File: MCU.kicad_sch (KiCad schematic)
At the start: 71 parts, among them J401 EXPANSION_PORT, J402 RS485_1, J403 RS485_2, J404 Conn_ARM_JTAG_SWD_10, U401 74HC4094, U402 74HC4094, U403 EFM32PG22C200F512IM40, U404 SN75176AD, U405 XC6204B33, Y401 Abracon_ABM11

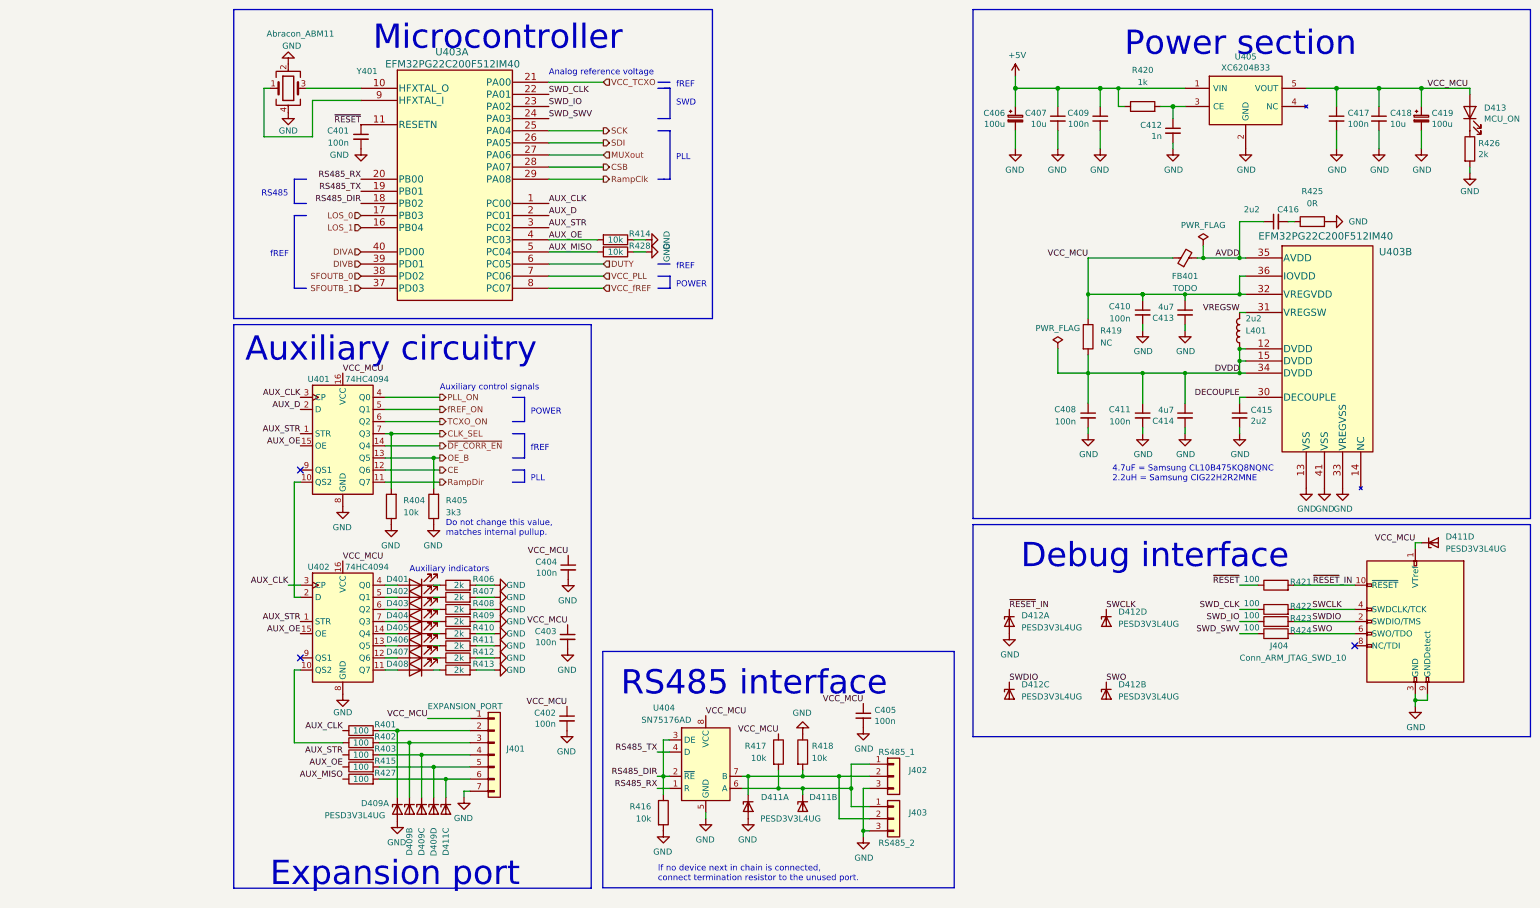
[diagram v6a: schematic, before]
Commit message: Partially reworked aux interface, about to be remade once again.
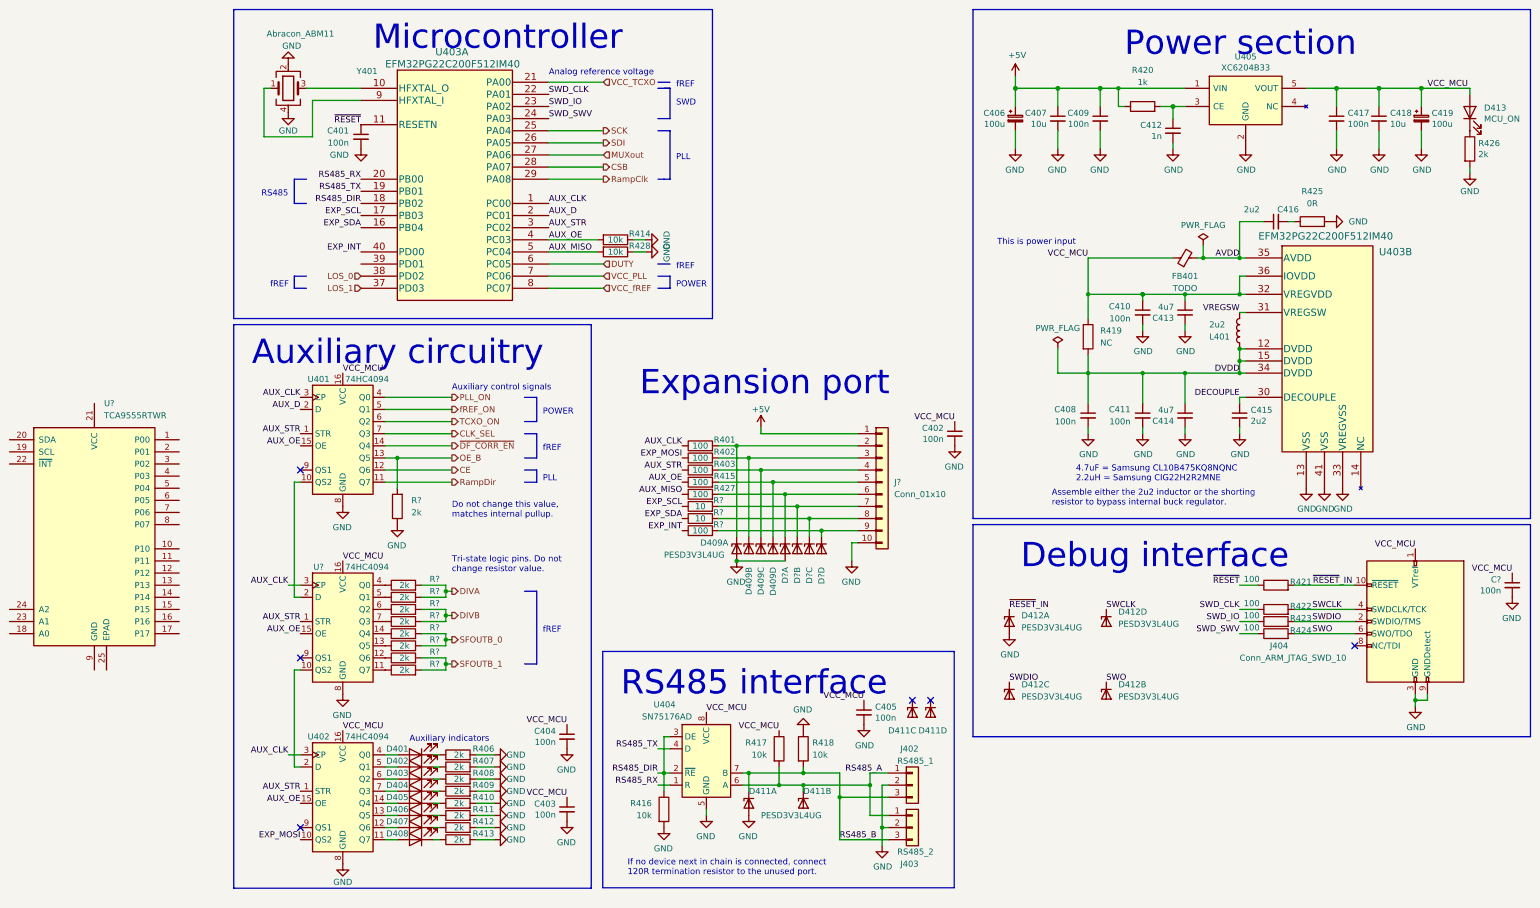
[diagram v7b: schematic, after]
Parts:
- removed J401: EXPANSION_PORT, Connector_PinHeader_2.54mm:PinHeader_1x07_P2.54mm_Vertical, symbol Connector_Generic:Conn_01x07
- removed R404: 10k, Resistor_SMD:R_0603_1608Metric_Pad0.98x0.95mm_HandSolder, symbol Device:R
- removed R405: 3k3, Resistor_SMD:R_0603_1608Metric_Pad0.98x0.95mm_HandSolder, symbol Device:R
- added C?: 100n, Capacitor_SMD:C_0603_1608Metric_Pad1.08x0.95mm_HandSolder, symbol Device:C_Small
- added D? (x4): PESD3V3L4UG, Package_TO_SOT_SMD:SOT-353_SC-70-5, symbol Power_Protection:PESD3V3L4UG
- added J?: Conn_01x10, Connector_FFC-FPC:TE_1-84952-0_1x10-1MP_P1.0mm_Horizontal, symbol Connector_Generic:Conn_01x10
- added R?: 100, Resistor_SMD:R_0603_1608Metric_Pad0.98x0.95mm_HandSolder, symbol Device:R
- added R? (x9): 2k, Resistor_SMD:R_0603_1608Metric_Pad0.98x0.95mm_HandSolder, symbol Device:R
- added R? (x2): 10, Resistor_SMD:R_0603_1608Metric_Pad0.98x0.95mm_HandSolder, symbol Device:R
- added U?: 74HC4094, Package_SO:SO-16_3.9x9.9mm_P1.27mm, symbol petr:74HC4094
- added U?: TCA9555RTWR, Package_DFN_QFN:WQFN-24-1EP_4x4mm_P0.5mm_EP2.45x2.45mm, symbol Interface_Expansion:TCA9555RTWR
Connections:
- net +5V: now also J?.1 (Pin_1)
- net AUX_CLK: now also U?.3 (CP)
- net AUX_OE: now also U?.15 (OE)
- net AUX_STR: now also U?.1 (STR)
- net DIVA: now also R?.2, R?.2; no longer U403.40 (PD00)
- net DIVB: now also R?.2, R?.2; no longer U403.39 (PD01)
- net GND: now also J402.2 (Pin_2), J403.2 (Pin_2), C?.2, D?.2 (A), J?.10 (Pin_10), R?.1, U?.8 (GND); no longer J402.3 (Pin_3), J403.3 (Pin_3)
- net LOS_0: now also U403.38 (PD02); no longer U403.17 (PB03)
- net LOS_1: now also U403.37 (PD03); no longer U403.16 (PB04)
- net OE_B: now also R?.2
- net SFOUTB_0: now also R?.2, R?.2; no longer U403.38 (PD02)
- net SFOUTB_1: now also R?.2, R?.2; no longer U403.37 (PD03)
- net VCC_MCU: now also C?.1, U?.16 (VCC); no longer D411.5 (K4)
- net at D409.1 (K1), R401.2: now also J?.2 (Pin_2)
- net EXP_MOSI: now reaches R402.1, U402.10 (QS2)
- net at U402.2 (D): now also U?.10 (QS2); no longer U401.10 (QS2)
- net RS485_A: now reaches D411.3 (K2), J402.1 (Pin_1), J403.1 (Pin_1), R417.2, U404.6 (A)
- net at D409.4 (K3), R403.2: now also J?.4 (Pin_4)
- net RS485_B: now reaches D411.1 (K1), R418.2, U404.7 (B)
- net RS485_B: now also J402.3 (Pin_3), J403.3 (Pin_3); no longer J402.2 (Pin_2), J403.2 (Pin_2)
- net at D409.5 (K4), R415.2: now also J?.5 (Pin_5)
- net at D409.3 (K2), R402.2: now also J?.3 (Pin_3)
- net at R427.2: now also D?.1 (K1), J?.6 (Pin_6); no longer D411.4 (K3)
- new net: D?.5 (K4), J?.9 (Pin_9), R?.2
- new net: R?.1, U?.11 (Q7)
- new net: R?.1, U?.12 (Q6)
- new net: R?.1, U?.13 (Q5)
- new net: R?.1, U?.14 (Q4)
- new net: U401.10 (QS2), U?.2 (D)
- new net: R?.1, U?.4 (Q0)
- new net: R?.1, U?.5 (Q1)
- new net: R?.1, U?.6 (Q2)
- new net: R?.1, U?.7 (Q3)
- new net: D?.4 (K3), J?.8 (Pin_8), R?.2
- new net: D?.3 (K2), J?.7 (Pin_7), R?.2
- new net EXP_INT: R?.1, U403.40 (PD00)
- new net EXP_SCL: R?.1, U403.17 (PB03)
- new net EXP_SDA: R?.1, U403.16 (PB04)
- no-connect marks 3 -> 6
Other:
- note added: "Assemble either the 2u2 inductor or the shorting resistor to bypass internal buck regulator."
- note added: "If no device next in chain is connected, connect 120R termination resistor to the unused port."
- note added: "This is power input"
- note added: "Tri-state logic pins. Do not change resistor value."
- note removed: "If no device next in chain is connected, connect termination resistor to the unused port."
- moved on the sheet: C402, C403, C404, C405, D401, D402, D403, D404, D405, D406, D407, D408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

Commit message: Remade and simplified AUX/EXT section.
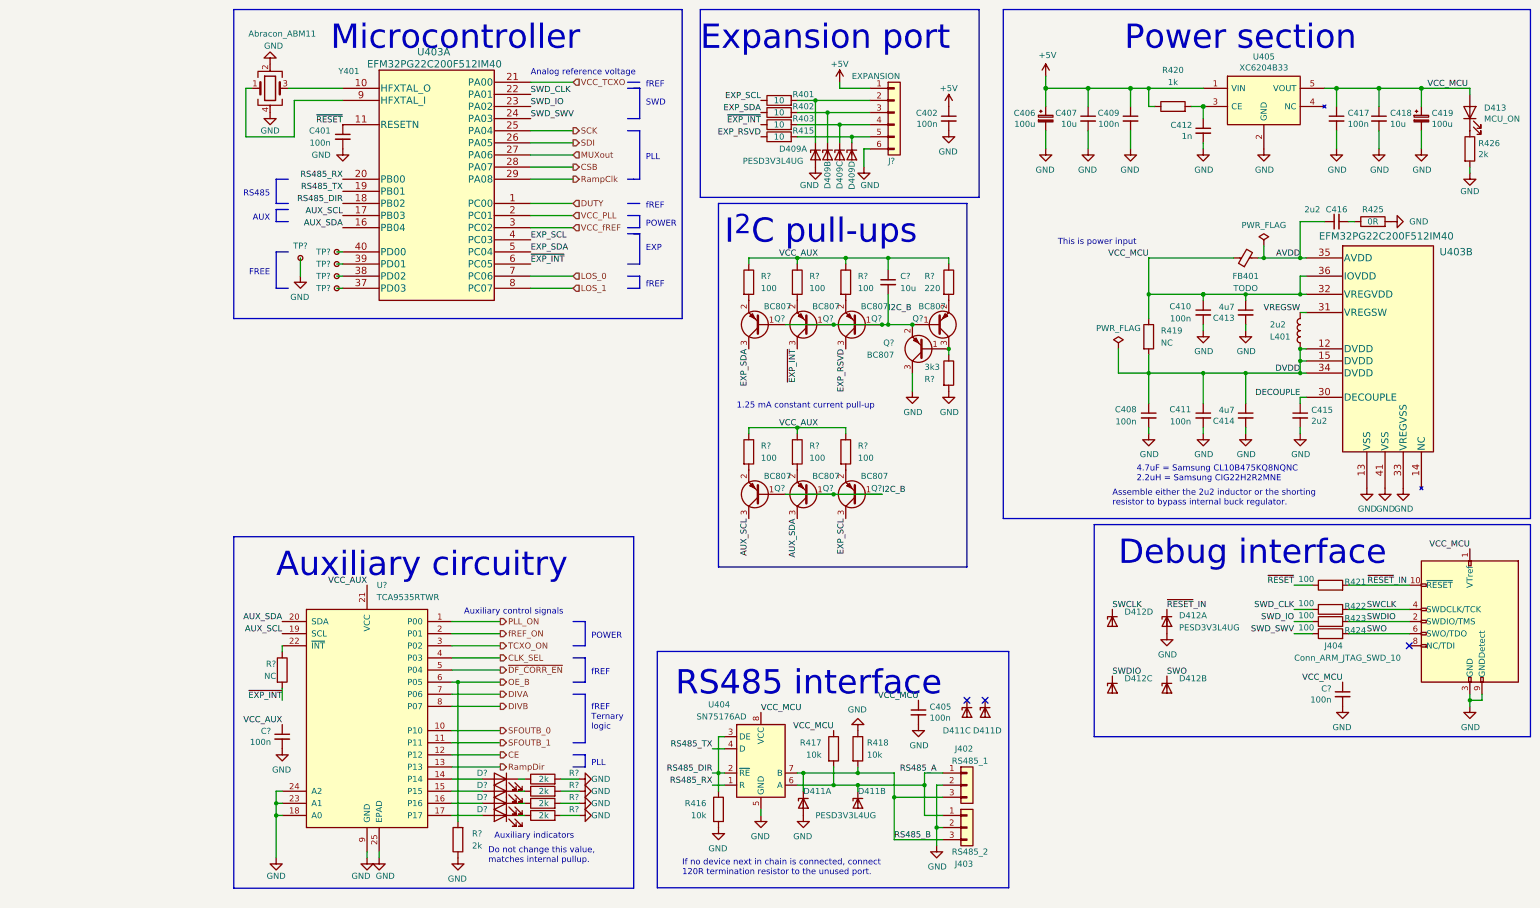
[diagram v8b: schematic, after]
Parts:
- removed C403, C404: 100n, Capacitor_SMD:C_0603_1608Metric_Pad1.08x0.95mm_HandSolder, symbol Device:C_Small
- removed D401, D402, D403, D404, D405, D406, D407, D408: (no value), LED_SMD:LED_0603_1608Metric_Pad1.05x0.95mm_HandSolder, symbol Device:LED
- removed D? (x4): PESD3V3L4UG, Package_TO_SOT_SMD:SOT-353_SC-70-5, symbol Power_Protection:PESD3V3L4UG
- removed J?: Conn_01x10, Connector_FFC-FPC:TE_1-84952-0_1x10-1MP_P1.0mm_Horizontal, symbol Connector_Generic:Conn_01x10
- removed R406, R407, R408, R409, R410, R411, R412, R413, R? (x9): 2k, Resistor_SMD:R_0603_1608Metric_Pad0.98x0.95mm_HandSolder, symbol Device:R
- removed R414, R428: 10k, Resistor_SMD:R_0603_1608Metric_Pad0.98x0.95mm_HandSolder, symbol Device:R
- removed R427, R?: 100, Resistor_SMD:R_0603_1608Metric_Pad0.98x0.95mm_HandSolder, symbol Device:R
- removed R? (x2): 10, Resistor_SMD:R_0603_1608Metric_Pad0.98x0.95mm_HandSolder, symbol Device:R
- removed U401, U402, U?: 74HC4094, Package_SO:SO-16_3.9x9.9mm_P1.27mm, symbol petr:74HC4094
- removed U?: TCA9555RTWR, Package_DFN_QFN:WQFN-24-1EP_4x4mm_P0.5mm_EP2.45x2.45mm, symbol Interface_Expansion:TCA9555RTWR
- added C?: 10u, Capacitor_SMD:C_0805_2012Metric_Pad1.18x1.45mm_HandSolder, symbol Device:C_Small
- added C?: 100n, Capacitor_SMD:C_0603_1608Metric_Pad1.08x0.95mm_HandSolder, symbol Device:C_Small
- added D? (x4): (no value), LED_SMD:LED_0603_1608Metric_Pad1.05x0.95mm_HandSolder, symbol Device:LED
- added J?: EXPANSION, Connector_FFC-FPC:TE_84952-6_1x06-1MP_P1.0mm_Horizontal, symbol Connector_Generic:Conn_01x06
- added Q? (x8): BC807, Package_TO_SOT_SMD:SOT-23, symbol Transistor_BJT:BC807
- added R?: NC, Resistor_SMD:R_0603_1608Metric_Pad0.98x0.95mm_HandSolder, symbol Device:R
- added R? (x6): 100, Resistor_SMD:R_0603_1608Metric_Pad0.98x0.95mm_HandSolder, symbol Device:R
- added R? (x5): 2k, Resistor_SMD:R_0603_1608Metric_Pad0.98x0.95mm_HandSolder, symbol Device:R
- added R?: 3k3, Resistor_SMD:R_0603_1608Metric_Pad0.98x0.95mm_HandSolder, symbol Device:R
- added R?: 220, Resistor_SMD:R_0603_1608Metric_Pad0.98x0.95mm_HandSolder, symbol Device:R
- added TP? (x5): TestPoint_Small, symbol 4ms_Connector:TestPoint_Small
- added U?: TCA9535RTWR, Package_DFN_QFN:WQFN-24-1EP_4x4mm_P0.5mm_EP2.45x2.45mm, symbol Interface_Expansion:TCA9535RTWR
- R401, R402, R403, R415: value 100 -> 10
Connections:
- net AUX_D is gone; now on net VCC_PLL: U403.2 (PC01)
- net AUX_MISO is gone; now on net EXP_SDA: U403.5 (PC04)
- net EXP_MOSI is gone; now on net EXP_SDA: R402.1
- net +5V: now also C402.1, J?.1 (Pin_1)
- net CE: now also U?.12 (P12)
- net CLK_SEL: now also U?.4 (P03)
- net DIVA: now also U?.7 (P06)
- net DIVB: now also U?.8 (P07)
- net DUTY: now also U403.1 (PC00); no longer U403.6 (PC05)
- net EXP_SCL: now also R401.1, U403.4 (PC03), Q?.3 (C); no longer U403.17 (PB03)
- net EXP_SDA: now also Q?.3 (C); no longer U403.16 (PB04)
- net GND: now also C?.2, J?.6 (Pin_6), Q?.3 (C), R?.1, R?.2, R?.2, R?.2, R?.2, R?.2, TP?.1, U?.18 (A0), U?.23 (A1), U?.24 (A2), U?.25 (EPAD), U?.9 (GND)
- net LOS_0: now also U403.7 (PC06); no longer U403.38 (PD02)
- net LOS_1: now also U403.8 (PC07); no longer U403.37 (PD03)
- net OE_B: now also R?.2, U?.6 (P05)
- net PLL_ON: now also U?.1 (P00)
- net RampDir: now also U?.13 (P13)
- net SFOUTB_0: now also U?.10 (P10)
- net SFOUTB_1: now also U?.11 (P11)
- net TCXO_ON: now also U?.3 (P02)
- net VCC_MCU: no longer C402.1
- net VCC_PLL: no longer U403.7 (PC06)
- net VCC_fREF: now also U403.3 (PC02); no longer U403.8 (PC07)
- net fREF_ON: now also U?.2 (P01)
- net ~{DF_CORR_EN}: now also U?.5 (P04)
- net at D409.1 (K1), R401.2: now also J?.2 (Pin_2)
- net at D409.4 (K3), R403.2: now also J?.4 (Pin_4)
- net at U403.39 (PD01): now also TP?.1
- net at D409.5 (K4), R415.2: now also J?.5 (Pin_5)
- net at D409.3 (K2), R402.2: now also J?.3 (Pin_3)
- removed net AUX_CLK: R401.1, U403.1 (PC00)
- net AUX_OE renamed EXP_RSVD
- net EXP_RSVD: now also Q?.3 (C); no longer U403.4 (PC03)
- net AUX_STR renamed ~{EXP_INT}
- net ~{EXP_INT}: now also U403.6 (PC05), Q?.3 (C), R?.2; no longer U403.3 (PC02)
- net EXP_INT: no longer names the net of U403.40 (PD00)
- net EXP_INT: now also TP?.1
- new net: R?.1, U?.22 (~{INT})
- new net: Q?.2 (E), R?.2 (x7)
- new net: TP?.1, U403.37 (PD03)
- new net: Q?.1 (B), Q?.3 (C), R?.1
- new net: TP?.1, U403.38 (PD02)
- new net: D?.1 (K), R?.1 (x4)
- new net: D?.2 (A), U?.15 (P15)
- new net: D?.2 (A), U?.16 (P16)
- new net: D?.2 (A), U?.14 (P14)
- new net: D?.2 (A), U?.17 (P17)
- new net AUX_SCL: Q?.3 (C), U403.17 (PB03), U?.19 (SCL)
- new net AUX_SDA: Q?.3 (C), U403.16 (PB04), U?.20 (SDA)
- new net I2C_B: C?.2, Q?.1 (B), Q?.1 (B), Q?.1 (B), Q?.1 (B), Q?.1 (B), Q?.1 (B), Q?.1 (B), Q?.2 (E)
- new net VCC_AUX: C?.1, C?.1, R?.1, R?.1, R?.1, R?.1, R?.1, R?.1, R?.1, U?.21 (VCC)
- no-connect marks 6 -> 3
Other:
- note added: "1.25 mA constant current pull-up"
- note added: "AUX"
- note added: "EXP"
- note added: "FREE"
- note added: "I^{2}C pull-ups"
- note added: "fREF Ternary logic"
- note removed: "Tri-state logic pins. Do not change resistor value."
- moved on the sheet: C401, C402, C405, C406, C407, C408, C409, C410, C411, C412, C413, C414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
